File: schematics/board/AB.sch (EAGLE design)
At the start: 65 parts

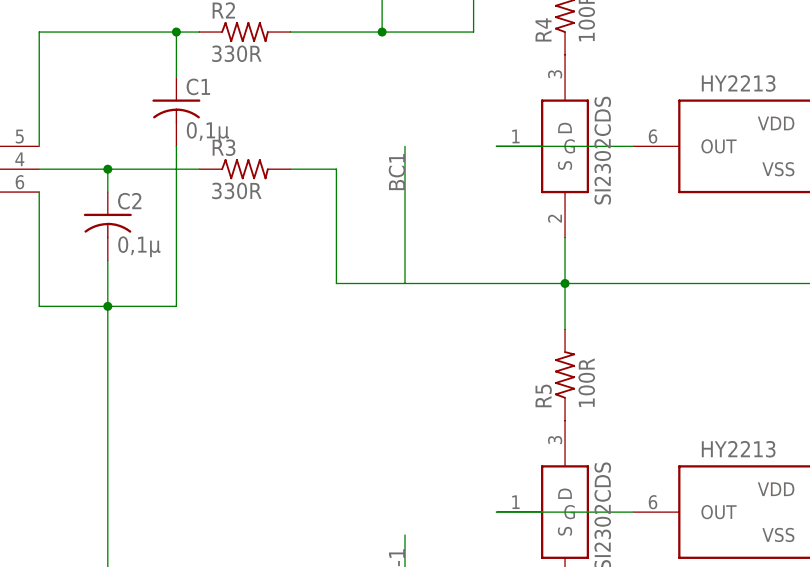
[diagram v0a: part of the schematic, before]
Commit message: Добавлены предохранители в библиотеку
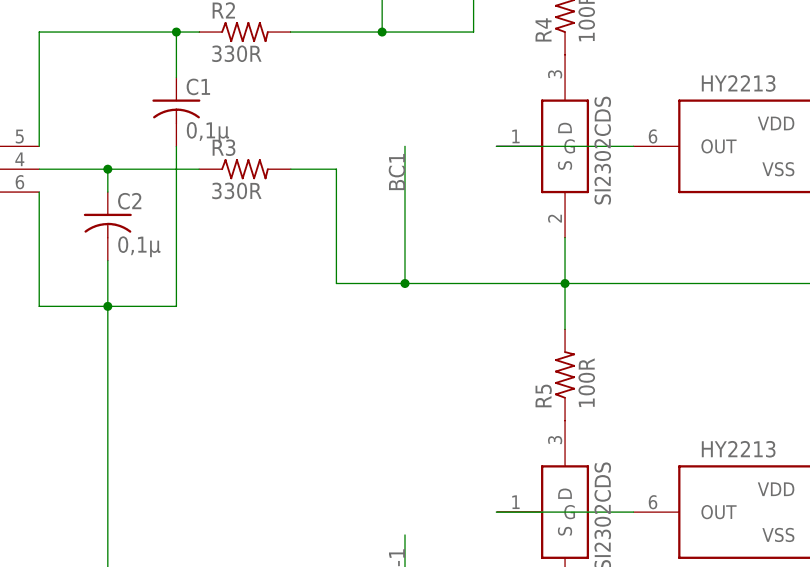
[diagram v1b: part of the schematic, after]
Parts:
- U$4, U$46, U$47, U$5: value HY2213 -> HY2213"; device CanCubeSat:HY2213 -> CanCubeSat:HY2213"
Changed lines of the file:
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@@
 <part name="B-2" library="CanCubeSat" deviceset="BATTERY" device=""/>
 <part name="U$3" library="CanCubeSat" deviceset="HY2120" device=""/>
-<part name="U$4" library="CanCubeSat" deviceset="HY2213" device=""/>
-<part name="U$5" library="CanCubeSat" deviceset="HY2213" device=""/>
+<part name="U$4" library="CanCubeSat" deviceset="HY2213" device="&quot;"/>
+<part name="U$5" library="CanCubeSat" deviceset="HY2213" device="&quot;"/>
 <part name="R1" library="resistor" library_urn="urn:adsk.eagle:library:348" deviceset="R-US_" device="R0603" package3d_urn="urn:adsk.eagle:package:23555/3" value="2k"/>
 <part name="R2" library="resistor" library_urn="urn:adsk.eagle:library:348" deviceset="R-US_" device="R0603" package3d_urn="urn:adsk.eagle:package:23555/3" value="330R"/>
@@
 <part name="R8" library="rcl" library_urn="urn:adsk.eagle:library:334" deviceset="R-US_" device="R2512" package3d_urn="urn:adsk.eagle:package:23545/2" value="R05"/>
 <part name="U$45" library="CanCubeSat" deviceset="HY2120" device=""/>
-<part name="U$46" library="CanCubeSat" deviceset="HY2213" device=""/>
-<part name="U$47" library="CanCubeSat" deviceset="HY2213" device=""/>
+<part name="U$46" library="CanCubeSat" deviceset="HY2213" device="&quot;"/>
+<part name="U$47" library="CanCubeSat" deviceset="HY2213" device="&quot;"/>
 <part name="R49" library="resistor" library_urn="urn:adsk.eagle:library:348" deviceset="R-US_" device="R0603" package3d_urn="urn:adsk.eagle:package:23555/3" value="2k"/>
 <part name="R50" library="resistor" library_urn="urn:adsk.eagle:library:348" deviceset="R-US_" device="R0603" package3d_urn="urn:adsk.eagle:package:23555/3" value="330R"/>
@@
 <label x="22.86" y="436.88" size="1.778" layer="95" rot="R90"/>
 <wire x1="22.86" y1="426.72" x2="22.86" y2="441.96" width="0.1524" layer="91"/>
+<junction x="22.86" y="426.72"/>
 </segment>
 </net>
@@
 </sheet>
 </sheets>
-<errors>
-</errors>
 </schematic>
 </drawing>

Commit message: Плата АB+DC-DC
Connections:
- net GND: now also R94.1, R95.1, R98.1, R99.1, U$10.CAT1, U$10.CAT2, U$2.CAT1, U$2.CAT2
- net NO_GND1: no longer R94.1, R95.1, U$2.CAT1, U$2.CAT2
- net NO_GND2: no longer R98.1, R99.1, U$10.CAT1, U$10.CAT2
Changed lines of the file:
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@@
 <junction x="149.86" y="386.08"/>
+</segment>
+<segment>
+<pinref part="U$2" gate="G$1" pin="CAT1"/>
+<wire x1="-91.44" y1="447.04" x2="-91.44" y2="457.2" width="0.1524" layer="91"/>
+<wire x1="-91.44" y1="457.2" x2="-91.44" y2="477.52" width="0.1524" layer="91"/>
+<wire x1="-91.44" y1="477.52" x2="-106.68" y2="477.52" width="0.1524" layer="91"/>
+<pinref part="U$2" gate="G$1" pin="CAT2"/>
+<wire x1="-101.6" y1="447.04" x2="-106.68" y2="447.04" width="0.1524" layer="91"/>
+<wire x1="-106.68" y1="447.04" x2="-106.68" y2="457.2" width="0.1524" layer="91"/>
+<pinref part="R95" gate="G$1" pin="1"/>
+<wire x1="-106.68" y1="457.2" x2="-106.68" y2="477.52" width="0.1524" layer="91"/>
+<junction x="-106.68" y="457.2"/>
+<pinref part="R94" gate="G$1" pin="1"/>
+<junction x="-91.44" y="457.2"/>
+<label x="-121.92" y="477.52" size="1.778" layer="95"/>
+<wire x1="-106.68" y1="477.52" x2="-121.92" y2="477.52" width="0.1524" layer="91"/>
+<junction x="-106.68" y="477.52"/>
+</segment>
+<segment>
+<pinref part="U$10" gate="G$1" pin="CAT1"/>
+<wire x1="198.12" y1="447.04" x2="198.12" y2="457.2" width="0.1524" layer="91"/>
+<wire x1="198.12" y1="457.2" x2="198.12" y2="480.06" width="0.1524" layer="91"/>
+<wire x1="198.12" y1="480.06" x2="182.88" y2="480.06" width="0.1524" layer="91"/>
+<pinref part="U$10" gate="G$1" pin="CAT2"/>
+<wire x1="187.96" y1="447.04" x2="182.88" y2="447.04" width="0.1524" layer="91"/>
+<wire x1="182.88" y1="447.04" x2="182.88" y2="457.2" width="0.1524" layer="91"/>
+<label x="167.64" y="480.06" size="1.778" layer="95"/>
+<wire x1="182.88" y1="457.2" x2="182.88" y2="480.06" width="0.1524" layer="91"/>
+<wire x1="182.88" y1="480.06" x2="167.64" y2="480.06" width="0.1524" layer="91"/>
+<junction x="182.88" y="480.06"/>
+<pinref part="R98" gate="G$1" pin="1"/>
+<junction x="198.12" y="457.2"/>
+<pinref part="R99" gate="G$1" pin="1"/>
+<junction x="182.88" y="457.2"/>
 </segment>
 </net>
@@
 <label x="-58.42" y="386.08" size="1.778" layer="95"/>
 </segment>
-<segment>
-<pinref part="U$2" gate="G$1" pin="CAT1"/>
-<wire x1="-91.44" y1="447.04" x2="-91.44" y2="457.2" width="0.1524" layer="91"/>
-<wire x1="-91.44" y1="457.2" x2="-91.44" y2="477.52" width="0.1524" layer="91"/>
-<wire x1="-91.44" y1="477.52" x2="-106.68" y2="477.52" width="0.1524" layer="91"/>
-<pinref part="U$2" gate="G$1" pin="CAT2"/>
-<wire x1="-101.6" y1="447.04" x2="-106.68" y2="447.04" width="0.1524" layer="91"/>
-<wire x1="-106.68" y1="447.04" x2="-106.68" y2="457.2" width="0.1524" layer="91"/>
-<pinref part="R95" gate="G$1" pin="1"/>
-<wire x1="-106.68" y1="457.2" x2="-106.68" y2="477.52" width="0.1524" layer="91"/>
-<junction x="-106.68" y="457.2"/>
-<pinref part="R94" gate="G$1" pin="1"/>
-<junction x="-91.44" y="457.2"/>
-<label x="-121.92" y="477.52" size="1.778" layer="95"/>
-<wire x1="-106.68" y1="477.52" x2="-121.92" y2="477.52" width="0.1524" layer="91"/>
-<junction x="-106.68" y="477.52"/>
-</segment>
 </net>
 <net name="N$10" class="0">
@@
 <label x="233.68" y="386.08" size="1.778" layer="95"/>
 </segment>
-<segment>
-<pinref part="U$10" gate="G$1" pin="CAT1"/>
-<wire x1="198.12" y1="447.04" x2="198.12" y2="457.2" width="0.1524" layer="91"/>
-<wire x1="198.12" y1="457.2" x2="198.12" y2="480.06" width="0.1524" layer="91"/>
-<wire x1="198.12" y1="480.06" x2="182.88" y2="480.06" width="0.1524" layer="91"/>
-<pinref part="U$10" gate="G$1" pin="CAT2"/>
-<wire x1="187.96" y1="447.04" x2="182.88" y2="447.04" width="0.1524" layer="91"/>
-<wire x1="182.88" y1="447.04" x2="182.88" y2="457.2" width="0.1524" layer="91"/>
-<label x="167.64" y="480.06" size="1.778" layer="95"/>
-<wire x1="182.88" y1="457.2" x2="182.88" y2="480.06" width="0.1524" layer="91"/>
-<wire x1="182.88" y1="480.06" x2="167.64" y2="480.06" width="0.1524" layer="91"/>
-<junction x="182.88" y="480.06"/>
-<pinref part="R98" gate="G$1" pin="1"/>
-<junction x="198.12" y="457.2"/>
-<pinref part="R99" gate="G$1" pin="1"/>
-<junction x="182.88" y="457.2"/>
-</segment>
-</net>
+</net>
